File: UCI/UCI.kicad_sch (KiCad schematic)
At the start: 8 parts, among them J1 Conn_02x14_Counter_Clockwise, U1 ESD224DQA

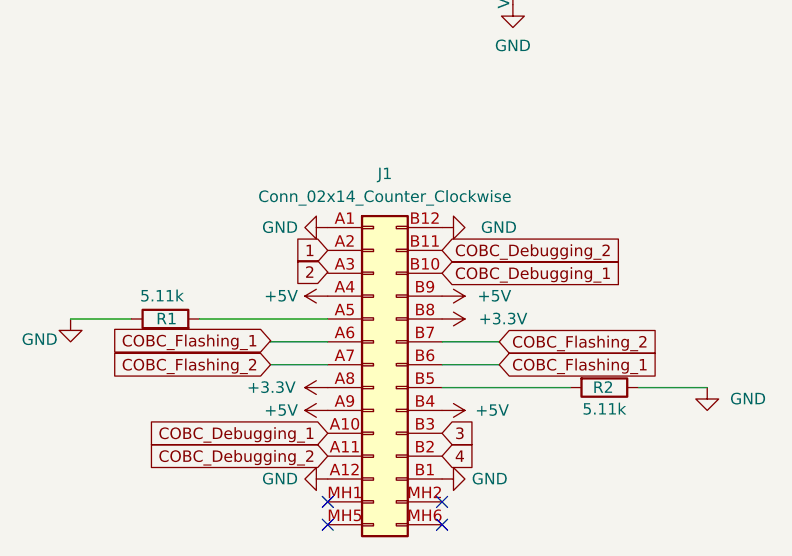
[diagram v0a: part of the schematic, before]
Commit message: Changed the layout of all the sidepanel PCBs to mitigate the problems that arised from the bad previous design.
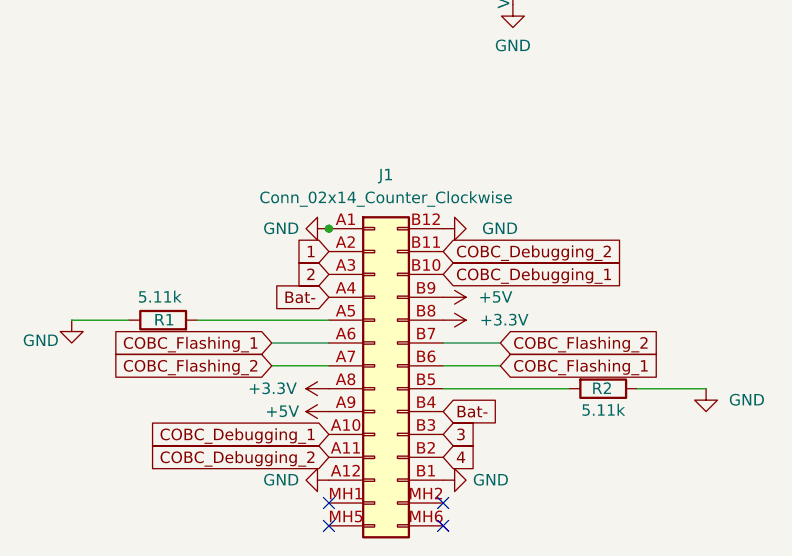
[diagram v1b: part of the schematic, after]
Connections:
- net +5V: no longer J1.A4 (Pin_4), J1.B4 (Pin_20)
- new net Bat-: J1.A4 (Pin_4), J1.B4 (Pin_20)

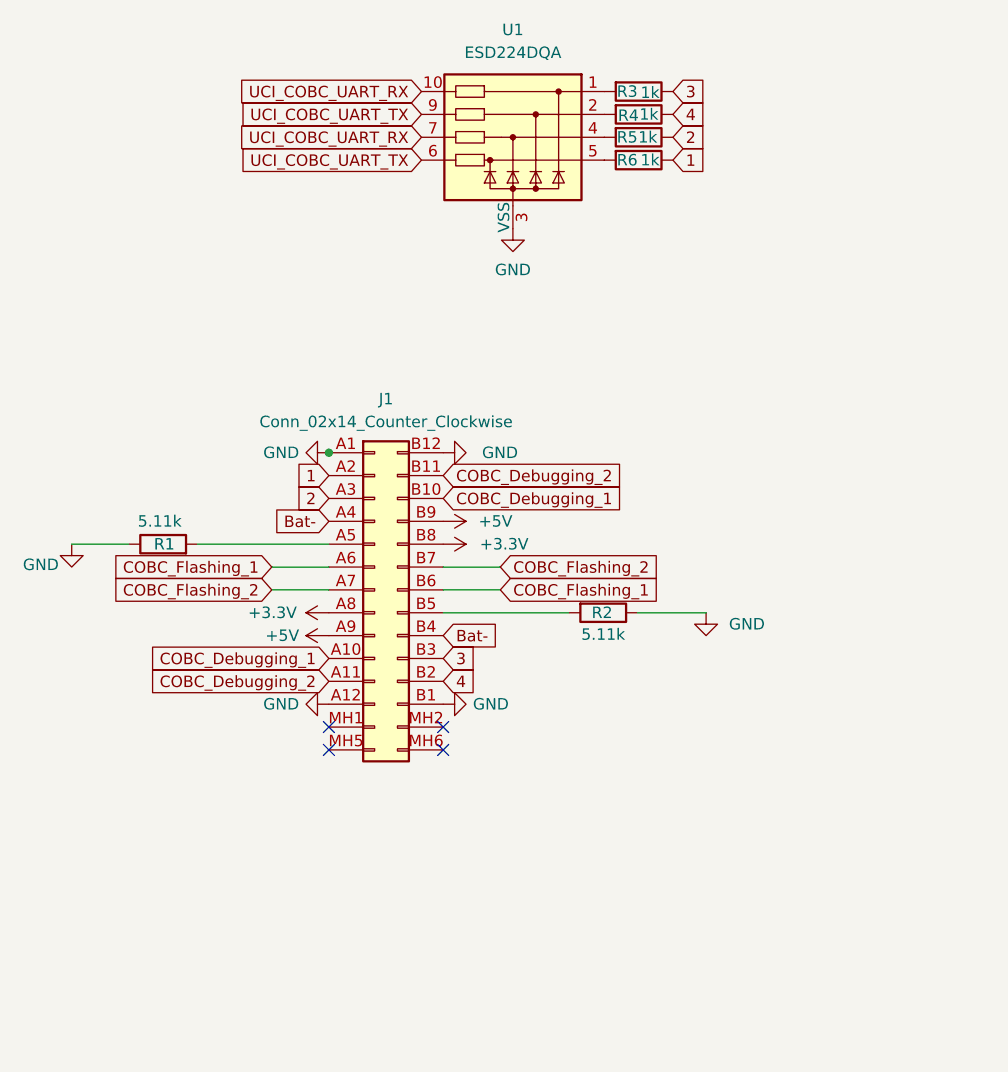
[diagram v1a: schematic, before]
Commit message: Added a  separate ground for the EDU  sensors and did  some small changes for ordering.
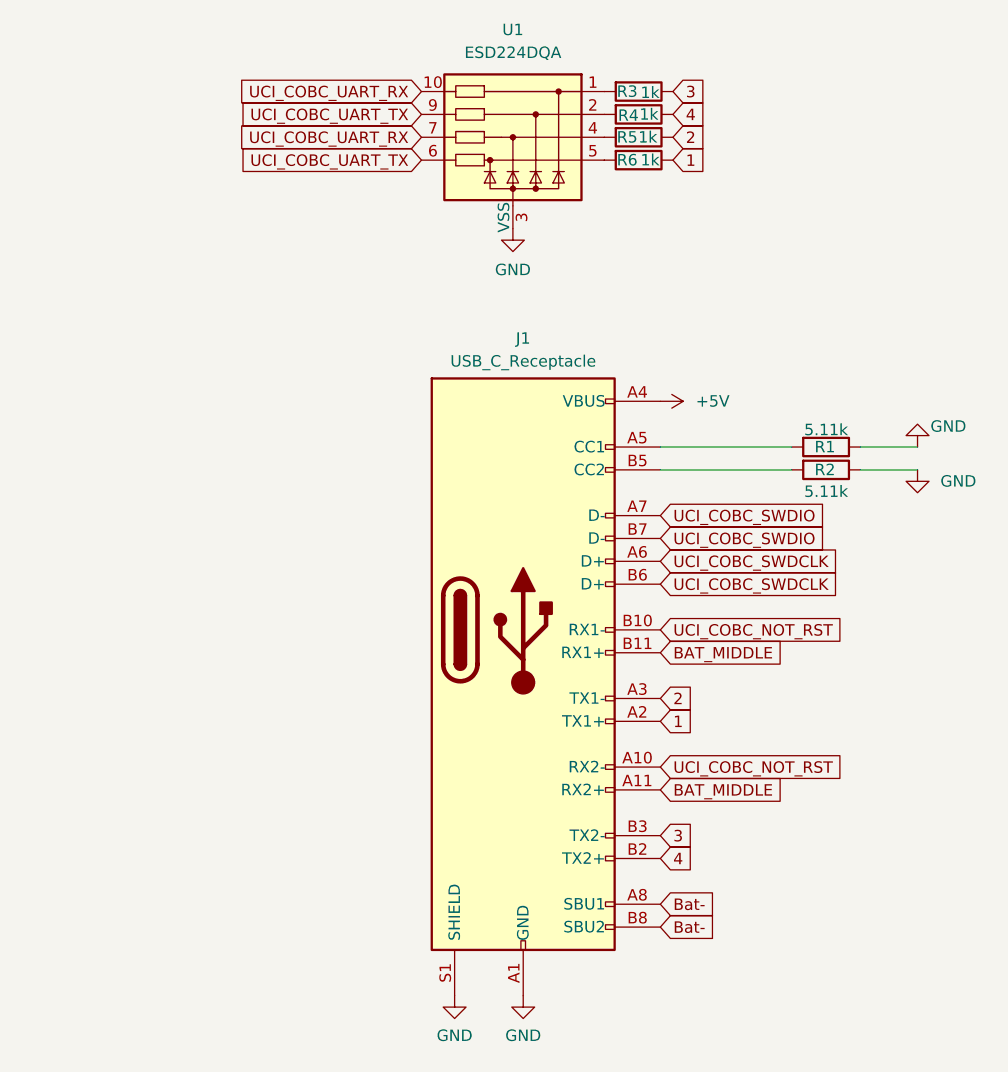
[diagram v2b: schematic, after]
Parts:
- removed J1: Conn_02x14_Counter_Clockwise, STS_connector:USB4160030170C, symbol Connector_Generic:Conn_02x14_Counter_Clockwise
- added J1: USB_C_Receptacle, STS_connector:USB4160030170C, symbol Connector:USB_C_Receptacle
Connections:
- net +5V: now also J1.A4 (VBUS), J1.A9 (VBUS), J1.B4 (VBUS), J1.B9 (VBUS)
- net 1: now also J1.A2 (TX1+)
- net 2: now also J1.A3 (TX1-)
- net 3: now also J1.B3 (TX2-)
- net 4: now also J1.B2 (TX2+)
- net Bat-: now also J1.A8 (SBU1), J1.B8 (SBU2)
- net GND: now also J1.A1 (GND), J1.A12 (GND), J1.B1 (GND), J1.B12 (GND), J1.S1 (SHIELD)
- net at R1.2: now also J1.A5 (CC1)
- net at R2.2: now also J1.B5 (CC2)
- new net BAT_MIDDLE: J1.A11 (RX2+), J1.B11 (RX1+)
- new net UCI_COBC_NOT_RST: J1.A10 (RX2-), J1.B10 (RX1-)
- new net UCI_COBC_SWDCLK: J1.A6 (D+), J1.B6 (D+)
- new net UCI_COBC_SWDIO: J1.A7 (D-), J1.B7 (D-)
- no-connect marks 4 -> 0
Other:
- moved on the sheet: R1, R2

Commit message: Commit before the order.
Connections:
- net BAT_MIDDLE is gone; now on net Bat-: J1.A11 (RX2+), J1.B11 (RX1+)
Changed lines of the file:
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@@
-    )
-  )
-  (global_label "BAT_MIDDLE" (shape input) (at 143.51 97.155 0) (fields_autoplaced)
-    (effects (font (size 1.27 1.27)) (justify left))
-    (property "Intersheetrefs" "${INTERSHEET_REFS}" (at 157.5623 97.155 0)
-      (effects (font (size 1.27 1.27)) (justify left) hide)
     )
   )
@@
     )
   )
-  (global_label "BAT_MIDDLE" (shape input) (at 143.51 112.395 0) (fields_autoplaced)
+  (global_label "Bat-" (shape input) (at 143.51 97.155 0) (fields_autoplaced)
     (effects (font (size 1.27 1.27)) (justify left))
-    (property "Intersheetrefs" "${INTERSHEET_REFS}" (at 157.5623 112.395 0)
+    (property "Intersheetrefs" "${INTERSHEET_REFS}" (at 151.2123 97.155 0)
       (effects (font (size 1.27 1.27)) (justify left) hide)
     )
@@
       (effects (font (size 1.27 1.27)) (justify left) hide)
     )
+  )
+  (global_label "Bat-" (shape input) (at 143.51 112.395 0) (fields_autoplaced)
+    (effects (font (size 1.27 1.27)) (justify left))
+    (property "Intersheetrefs" "${INTERSHEET_REFS}" (at 151.2123 112.395 0)
+      (effects (font (size 1.27 1.27)) (justify left) hide)
+    )

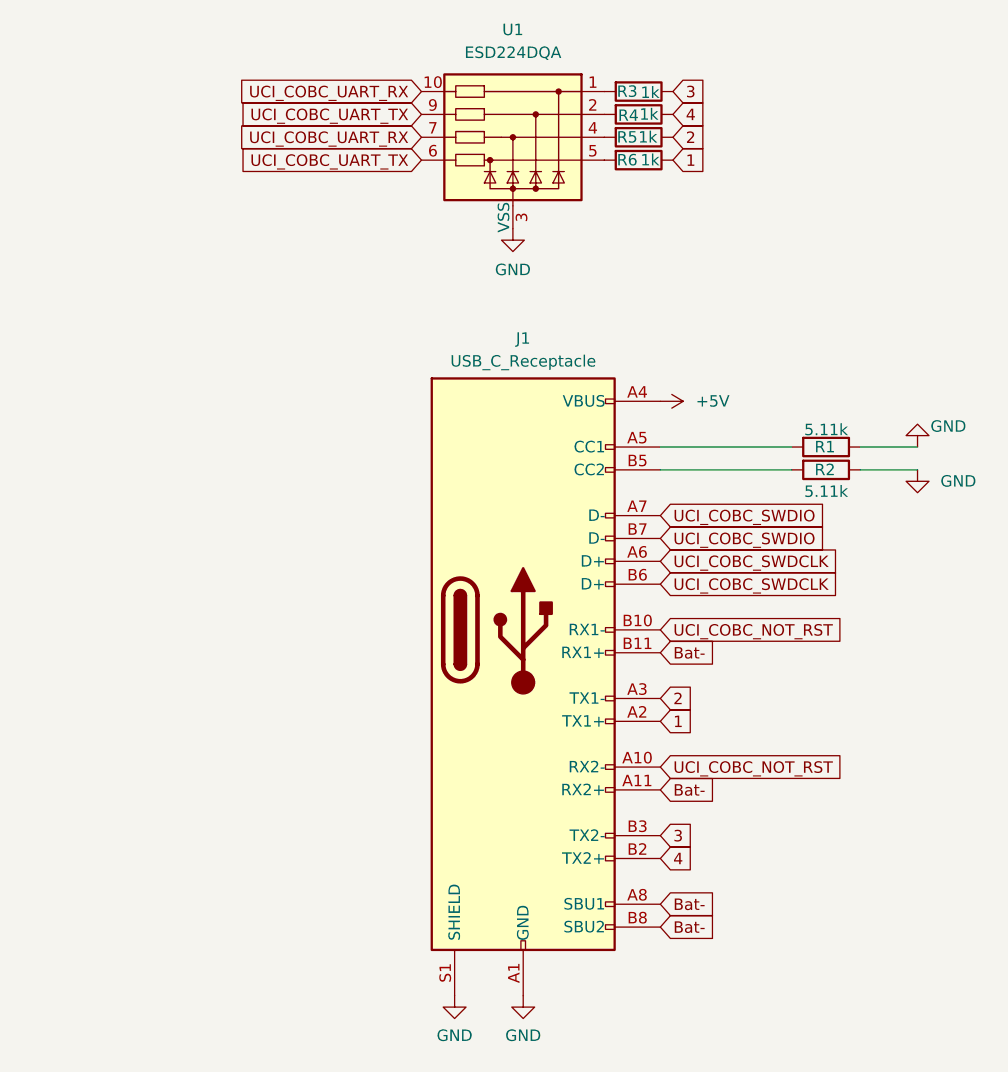
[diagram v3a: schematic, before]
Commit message: changed all vias from blind to trough and removed the unused pins of the uci connector
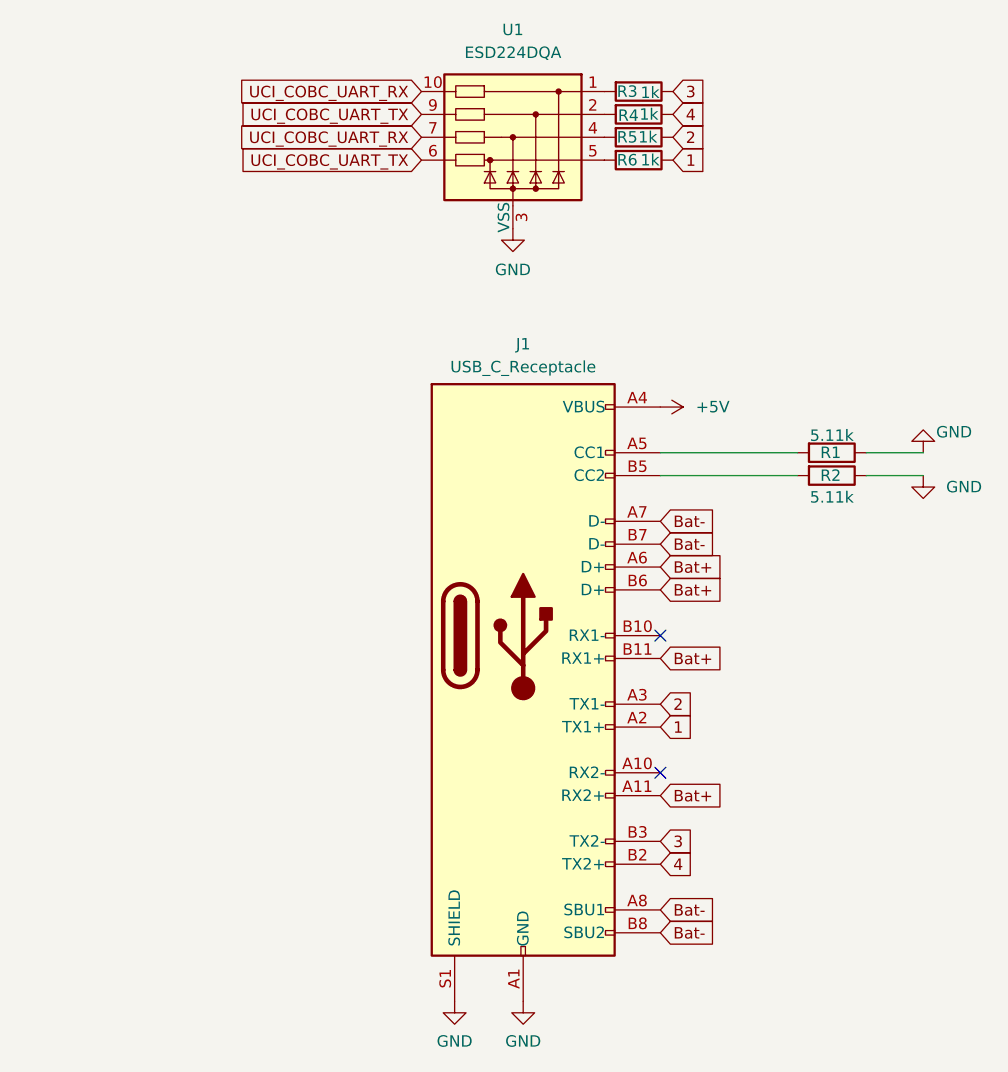
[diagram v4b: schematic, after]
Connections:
- net UCI_COBC_SWDIO is gone; now on net Bat-: J1.A7 (D-), J1.B7 (D-)
- net Bat-: no longer J1.A11 (RX2+), J1.B11 (RX1+)
- net UCI_COBC_NOT_RST: no longer names the net of J1.A10 (RX2-)
- net UCI_COBC_NOT_RST: no longer J1.B10 (RX1-)
- net UCI_COBC_SWDCLK renamed Bat+
- net Bat+: now also J1.A11 (RX2+), J1.B11 (RX1+)
- no-connect marks 0 -> 2
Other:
- moved on the sheet: J1, R1, R2
